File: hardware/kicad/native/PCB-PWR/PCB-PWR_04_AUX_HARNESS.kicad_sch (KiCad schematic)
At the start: 9 parts, among them J2 MAIN_PWR_43045-1202_12PIN, U5 TPS7A2018PDBVR 1V8_MIC

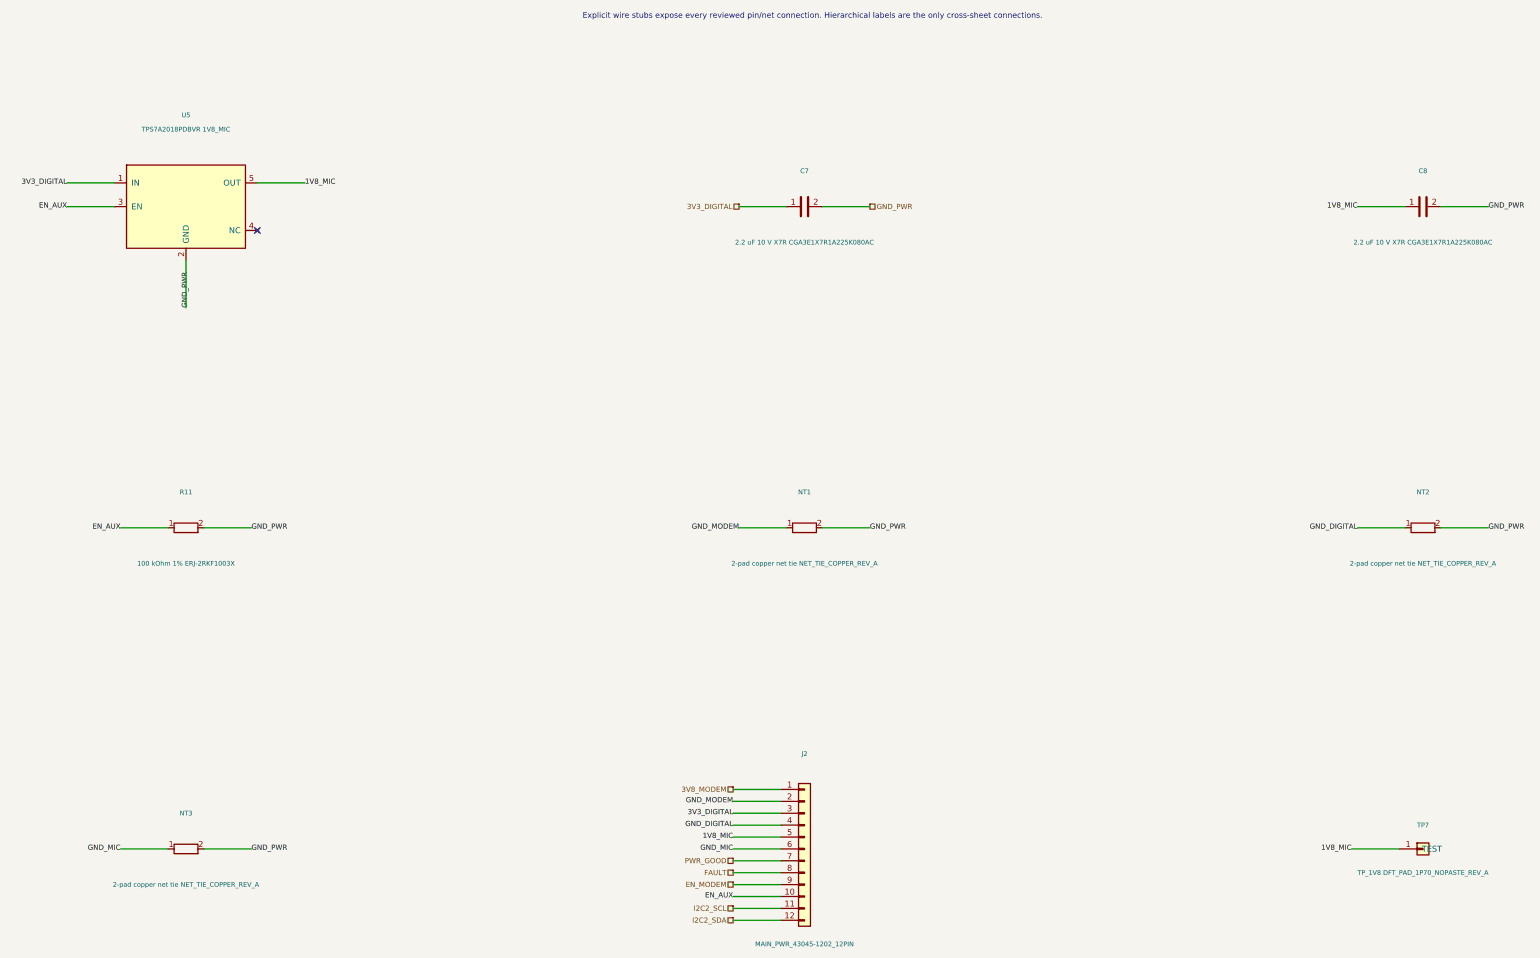
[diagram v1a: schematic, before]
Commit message: pcb-pwr: keep labels clear of connection wires
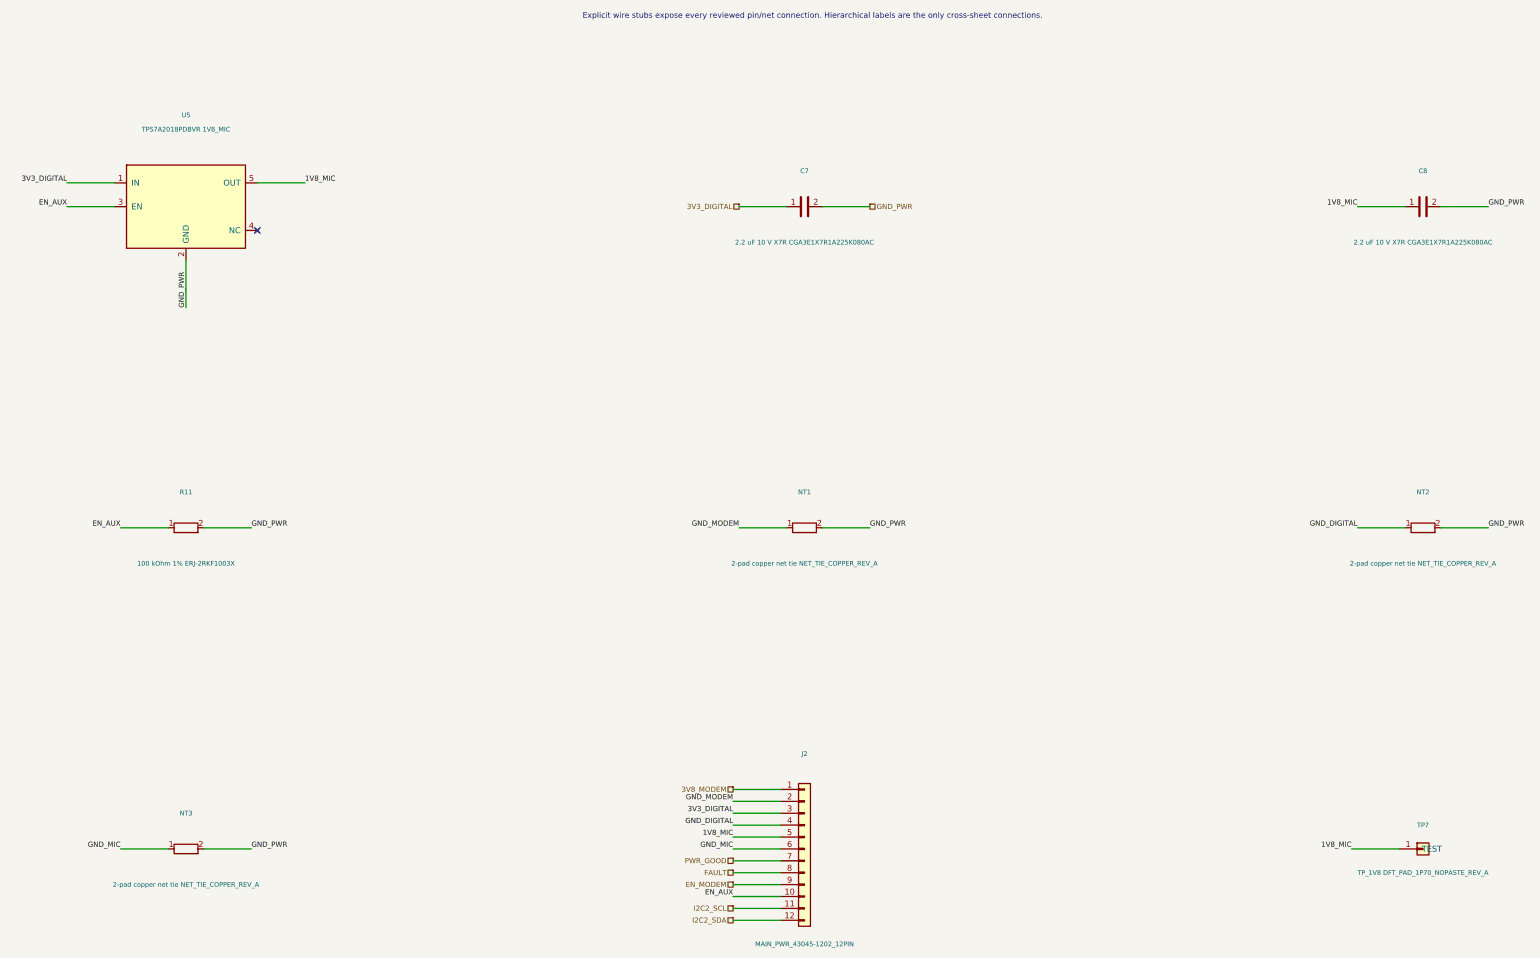
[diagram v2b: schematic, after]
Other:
- title: Dioneya EVT-PRE-20 PCB-PWR Rev.A - 1V8 auxiliary and MAIN harness -> 1V8 + MAIN harness
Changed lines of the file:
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@@
   (paper "A3")
   (title_block
-    (title "Dioneya EVT-PRE-20 PCB-PWR Rev.A - 1V8 auxiliary and MAIN harness")
+    (title "1V8 + MAIN harness")
     (date "2026-09-17")
     (rev "A")
@@
   )
   (label "1V8_MIC" (at 326.39 60.96 180)
-    (effects (font (size 1.1 1.1)))
+    (effects (font (size 1.1 1.1)) (justify bottom))
   )
   (label "GND_PWR" (at 354.33 60.96 0)
-    (effects (font (size 1.1 1.1)))
+    (effects (font (size 1.1 1.1)) (justify bottom))
   )
   (label "GND_MODEM" (at 193.04 187.96 180)
-    (effects (font (size 1.1 1.1)))
+    (effects (font (size 1.1 1.1)) (justify bottom))
   )
   (label "3V3_DIGITAL" (at 193.04 190.5 180)
-    (effects (font (size 1.1 1.1)))
+    (effects (font (size 1.1 1.1)) (justify bottom))
   )
   (label "GND_DIGITAL" (at 193.04 193.04 180)
-    (effects (font (size 1.1 1.1)))
+    (effects (font (size 1.1 1.1)) (justify bottom))
   )
   (label "1V8_MIC" (at 193.04 195.58 180)
-    (effects (font (size 1.1 1.1)))
+    (effects (font (size 1.1 1.1)) (justify bottom))
   )
   (label "GND_MIC" (at 193.04 198.12 180)
-    (effects (font (size 1.1 1.1)))
+    (effects (font (size 1.1 1.1)) (justify bottom))
   )
   (label "EN_AUX" (at 193.04 208.28 180)
-    (effects (font (size 1.1 1.1)))
+    (effects (font (size 1.1 1.1)) (justify bottom))
   )
   (label "GND_MODEM" (at 194.31 129.54 180)
-    (effects (font (size 1.1 1.1)))
+    (effects (font (size 1.1 1.1)) (justify bottom))
   )
   (label "GND_PWR" (at 222.25 129.54 0)
-    (effects (font (size 1.1 1.1)))
+    (effects (font (size 1.1 1.1)) (justify bottom))
   )
   (label "GND_DIGITAL" (at 326.39 129.54 180)
-    (effects (font (size 1.1 1.1)))
+    (effects (font (size 1.1 1.1)) (justify bottom))
   )
   (label "GND_PWR" (at 354.33 129.54 0)
-    (effects (font (size 1.1 1.1)))
+    (effects (font (size 1.1 1.1)) (justify bottom))
   )
   (label "GND_MIC" (at 62.23 198.12 180)
-    (effects (font (size 1.1 1.1)))
+    (effects (font (size 1.1 1.1)) (justify bottom))
   )
   (label "GND_PWR" (at 90.17 198.12 0)
-    (effects (font (size 1.1 1.1)))
+    (effects (font (size 1.1 1.1)) (justify bottom))
   )
   (label "EN_AUX" (at 62.23 129.54 180)
-    (effects (font (size 1.1 1.1)))
+    (effects (font (size 1.1 1.1)) (justify bottom))
   )
   (label "GND_PWR" (at 90.17 129.54 0)
-    (effects (font (size 1.1 1.1)))
+    (effects (font (size 1.1 1.1)) (justify bottom))
   )
   (label "1V8_MIC" (at 325.12 198.12 180)
-    (effects (font (size 1.1 1.1)))
+    (effects (font (size 1.1 1.1)) (justify bottom))
   )
   (label "3V3_DIGITAL" (at 50.8 55.88 180)
-    (effects (font (size 1.1 1.1)))
+    (effects (font (size 1.1 1.1)) (justify bottom))
   )
   (label "GND_PWR" (at 76.2 82.55 90)
-    (effects (font (size 1.1 1.1)))
+    (effects (font (size 1.1 1.1)) (justify bottom))
   )
   (label "EN_AUX" (at 50.8 60.96 180)
-    (effects (font (size 1.1 1.1)))
+    (effects (font (size 1.1 1.1)) (justify bottom))
   )
   (label "1V8_MIC" (at 101.6 55.88 0)
-    (effects (font (size 1.1 1.1)))
+    (effects (font (size 1.1 1.1)) (justify bottom))
   )
   (hierarchical_label "3V3_DIGITAL" (shape passive) (at 194.31 60.96 180)
-    (effects (font (size 1.1 1.1)))
+    (effects (font (size 1.1 1.1)) (justify bottom))
   )
   (hierarchical_label "GND_PWR" (shape passive) (at 222.25 60.96 0)
-    (effects (font (size 1.1 1.1)))
+    (effects (font (size 1.1 1.1)) (justify bottom))
   )
   (hierarchical_label "3V8_MODEM" (shape passive) (at 193.04 185.42 180)
-    (effects (font (size 1.1 1.1)))
+    (effects (font (size 1.1 1.1)) (justify bottom))
   )
   (hierarchical_label "PWR_GOOD" (shape passive) (at 193.04 200.66 180)
-    (effects (font (size 1.1 1.1)))
+    (effects (font (size 1.1 1.1)) (justify bottom))
   )
   (hierarchical_label "FAULT" (shape passive) (at 193.04 203.2 180)
-    (effects (font (size 1.1 1.1)))
+    (effects (font (size 1.1 1.1)) (justify bottom))
   )
   (hierarchical_label "EN_MODEM" (shape passive) (at 193.04 205.74 180)
-    (effects (font (size 1.1 1.1)))
+    (effects (font (size 1.1 1.1)) (justify bottom))
   )
   (hierarchical_label "I2C2_SCL" (shape passive) (at 193.04 210.82 180)
-    (effects (font (size 1.1 1.1)))
+    (effects (font (size 1.1 1.1)) (justify bottom))
   )
   (hierarchical_label "I2C2_SDA" (shape passive) (at 193.04 213.36 180)
-    (effects (font (size 1.1 1.1)))
+    (effects (font (size 1.1 1.1)) (justify bottom))
   )
   (symbol (lib_id "Device:C") (at 208.28 60.96 90) (unit 1)
